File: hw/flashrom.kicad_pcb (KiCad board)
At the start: 2 copper layers, 22.9 x 52.1 mm, 12 parts, among them J1 Conn_01x03_Male, J3 Conn_01x03_Male, U1 Kickstart_Socket_A4000, U2 29F800

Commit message: convert project to kicad 7 format
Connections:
- net /~CE renamed /~{CE}
- net /~OE renamed /~{OE}
- net /~RESET renamed /~{RESET}
- net /~WE renamed /~{WE}
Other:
- net class Default removed
- board text added: "~{BUSY }WE ~{RESET}"
- board text removed: "~BUSY ~WE ~RESET"

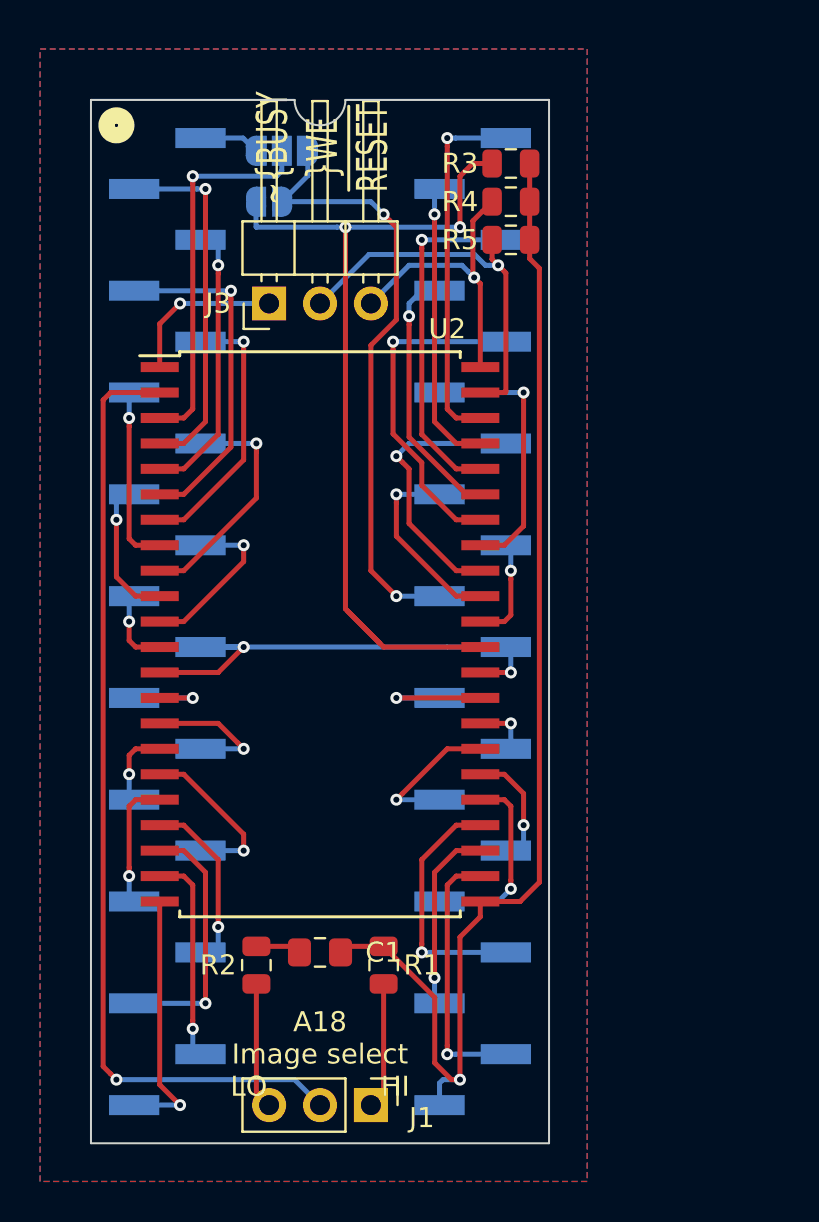
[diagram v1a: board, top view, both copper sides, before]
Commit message: switch flash to tsop, add tvs, and route pcb
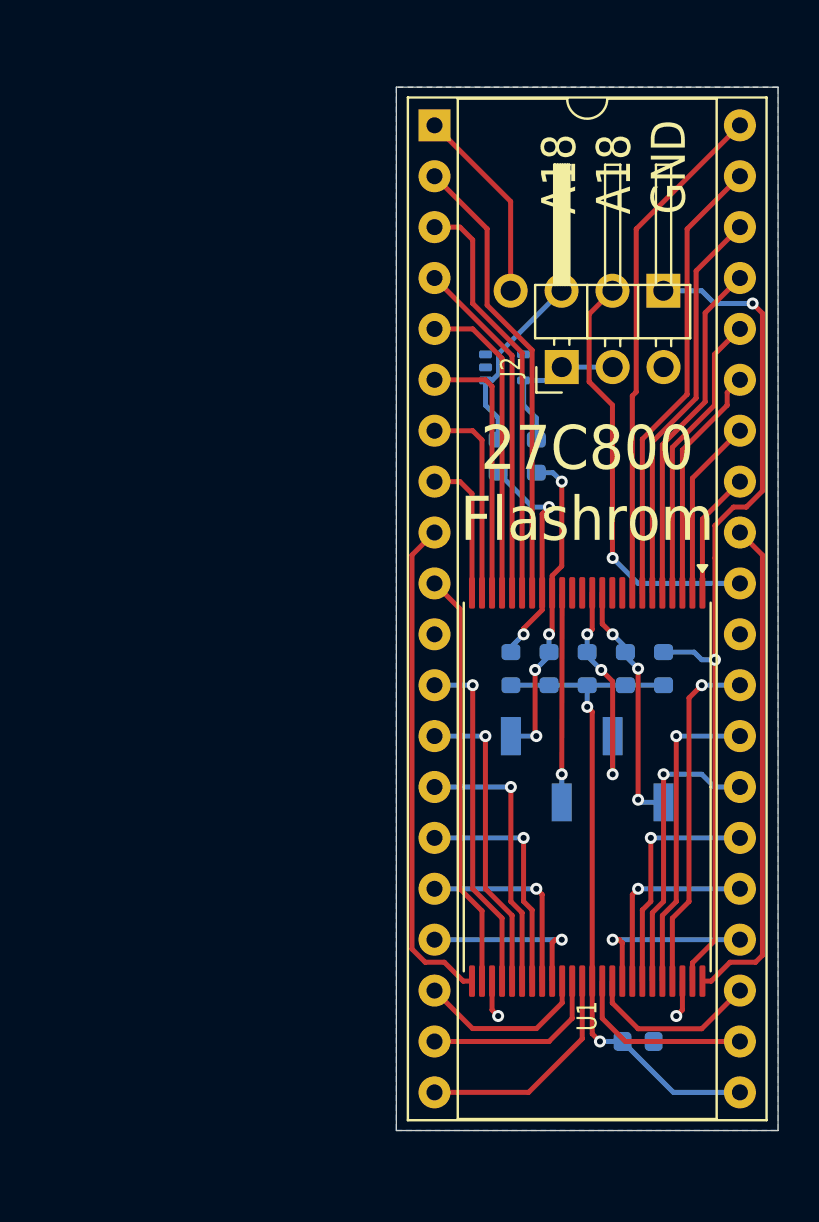
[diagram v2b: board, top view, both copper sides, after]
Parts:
- removed JP1: SolderJumper_3_Bridged12, Jumper:SolderJumper-3_P1.3mm_Open_RoundedPad1.0x1.5mm
- removed JP2: SolderJumper_2_Bridged, Jumper:SolderJumper-2_P1.3mm_Open_RoundedPad1.0x1.5mm
- added D1: NSQA6V8AW5T2G, Package_TO_SOT_SMD:SOT-353_SC-70-5, B.Cu at (54.3, 62.9)
- added J2: Conn_01x03_Pin, Connector_PinHeader_2.54mm:PinHeader_1x03_P2.54mm_Horizontal, F.Cu at (57.1, 62.9)
- added R6: 15k, Resistor_SMD:R_0603_1608Metric, B.Cu at (56.5, 77.9)
- added R7: 15k, Resistor_SMD:R_0603_1608Metric, B.Cu at (54.6, 77.9)
- C1: footprint Capacitor_SMD:C_0805_2012Metric_Pad1.15x1.40mm_HandSolder -> Capacitor_SMD:C_0603_1608Metric; moved to B.Cu
- J1: value Conn_01x03_Male -> Conn_01x04_Pin; footprint Connector_PinHeader_2.54mm:PinHeader_1x03_P2.54mm_Vertical -> Connector_PinHeader_2.54mm:PinHeader_1x04_P2.54mm_Horizontal; moved to B.Cu
- J3: value Conn_01x03_Male -> BG306-04-A-1-0400-L; footprint Connector_PinHeader_2.54mm:PinHeader_1x03_P2.54mm_Horizontal -> Connector_PinSocket_2.54mm:PinSocket_1x04_P2.54mm_Vertical_SMD_Pin1Left; moved to B.Cu
- R1, R2: value 10k -> 100; footprint Resistor_SMD:R_0805_2012Metric -> Resistor_SMD:R_0603_1608Metric; moved to B.Cu
- R3, R4, R5: value 10k -> 15k; footprint Resistor_SMD:R_0805_2012Metric -> Resistor_SMD:R_0603_1608Metric; moved to B.Cu
- U1: value Kickstart_Socket_A4000 -> 29F800-TSOP; footprint flashkick:DIP-40_W15.24mm_SMDHeader -> Package_SO:TSOP-I-48_18.4x12mm_P0.5mm; moved to F.Cu
- U2: value 29F800 -> Kickstart_Socket_A4000; footprint Package_SO:PSOP-44_16.9x27.17mm_P1.27mm -> Package_DIP:DIP-40_W15.24mm_Socket
- moved J1 43.2 mm to (62.2, 59.1), turned to 90 degrees
- moved R2 29.0 mm to (55.9, 67.3), turned to -90 degrees
- moved J3 28.1 mm to (58.4, 82.9)
- moved R3 26.3 mm to (62.2, 77.9), turned to -90 degrees
- moved U2 26.0 mm to (50.8, 50.8)
- moved R1 26.0 mm to (54.0, 67.3), turned to 90 degrees
- moved R4 24.0 mm to (60.3, 77.9), turned to -90 degrees
- moved R5 21.7 mm to (58.4, 77.9), turned to -90 degrees
- moved C1 16.5 mm to (61.0, 96.5), turned to 0 degrees
- moved U1 10.0 mm to (58.4, 83.8), turned to -90 degrees
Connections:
- J1 pad 1: Net-(J1-Pad1) -> /~{BYTE}
- J1 pad 2: /A18 -> /OA17
- J1 pad 3: Net-(J1-Pad3) -> /TVS1
- J3 pad 1: Net-(J3-Pad1) -> /~{WE}
- J3 pad 2: /~{WE} -> /~{RESET}
- J3 pad 3: /~{RESET} -> /RY/~{BY}
- R1 pad 1: +5V -> /A17
- R1 pad 2: Net-(J1-Pad1) -> /TVS1
- R2 pad 1: Net-(J1-Pad3) -> /TVS3
- R2 pad 2: GND -> /A18
- R3 pad 1: +5V -> /~{BYTE}
- R3 pad 2: Net-(JP2-Pad1) -> +5V
- R4 pad 1: +5V -> /~{WE}
- R4 pad 2: /~{RESET} -> +5V
- R5 pad 1: +5V -> /~{RESET}
- R5 pad 2: /~{WE} -> +5V
- U1 pad 1: /NA17 -> /A15
- U1 pad 10: /~{CE} -> unconnected-(U1-NC-Pad10)
- U1 pad 11: GND -> /~{WE}
- U1 pad 12: /~{OE} -> /~{RESET}
- U1 pad 13: /D0 -> unconnected-(U1-NC-Pad13)
- U1 pad 14: /D8 -> unconnected-(U1-NC-Pad14)
- U1 pad 15: /D1 -> /RY/~{BY}
- U1 pad 16: /D9 -> /A18
- U1 pad 17: /D2 -> /A17
- U1 pad 18: /D10 -> /A7
- U1 pad 19: /D3 -> /A6
- U1 pad 2: /A7 -> /A14
- U1 pad 20: /D11 -> /A5
- U1 pad 21: +5V -> /A4
- U1 pad 22: /D4 -> /A3
- U1 pad 23: /D12 -> /A2
- U1 pad 24: /D5 -> /A1
- U1 pad 25: /D13 -> /A0
- U1 pad 26: /D6 -> /~{CE}
- U1 pad 27: /D14 -> GND
- U1 pad 28: /D7 -> /~{OE}
- U1 pad 29: /D15 -> /D0
- U1 pad 3: /A6 -> /A13
- U1 pad 30: GND -> /D8
- U1 pad 31: /OA17 -> /D1
- U1 pad 32: /A16 -> /D9
- U1 pad 33: /A15 -> /D2
- U1 pad 34: /A14 -> /D10
- U1 pad 35: /A13 -> /D3
- U1 pad 36: /A12 -> /D11
- U1 pad 37: /A11 -> +5V
- U1 pad 38: /A10 -> /D4
- U1 pad 39: /A9 -> /D12
- U1 pad 4: /A5 -> /A12
- U1 pad 40: /A8 -> /D5
- U1 pad 5: /A4 -> /A11
- U1 pad 6: /A3 -> /A10
- U1 pad 7: /A2 -> /A9
- U1 pad 8: /A1 -> /A8
- U1 pad 9: /A0 -> unconnected-(U1-NC-Pad9)
- U2 pad 1: Net-(J3-Pad1) -> /NA17
- U2 pad 10: /A1 -> /~{CE}
- U2 pad 11: /A0 -> GND
- U2 pad 12: /~{CE} -> /~{OE}
- U2 pad 13: GND -> /D0
- U2 pad 14: /~{OE} -> /D8
- U2 pad 15: /D0 -> /D1
- U2 pad 16: /D8 -> /D9
- U2 pad 17: /D1 -> /D2
- U2 pad 18: /D9 -> /D10
- U2 pad 19: /D2 -> /D3
- U2 pad 2: /A18 -> /A7
- U2 pad 20: /D10 -> /D11
- U2 pad 21: /D3 -> +5V
- U2 pad 22: /D11 -> /D4
- U2 pad 23: +5V -> /D12
- U2 pad 24: /D4 -> /D5
- U2 pad 25: /D12 -> /D13
- U2 pad 26: /D5 -> /D6
- U2 pad 27: /D13 -> /D14
- U2 pad 28: /D6 -> /D7
- U2 pad 29: /D14 -> /D15
- U2 pad 3: /A17 -> /A6
- U2 pad 30: /D7 -> GND
- U2 pad 31: /D15 -> /OA17
- U2 pad 32: GND -> /A16
- U2 pad 33: Net-(JP2-Pad1) -> /A15
- U2 pad 34: /A16 -> /A14
- U2 pad 35: /A15 -> /A13
- U2 pad 36: /A14 -> /A12
- U2 pad 37: /A13 -> /A11
- U2 pad 38: /A12 -> /A10
- U2 pad 39: /A11 -> /A9
- U2 pad 4: /A7 -> /A5
- U2 pad 40: /A10 -> /A8
- U2 pad 5: /A6 -> /A4
- U2 pad 6: /A5 -> /A3
- U2 pad 7: /A4 -> /A2
- U2 pad 8: /A3 -> /A1
- U2 pad 9: /A2 -> /A0
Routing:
- net Net-(JP2-Pad1): track 44.7 -> 0.00 mm, vias 2 -> 0
- net /~{BYTE}: track 0.00 -> 43.3 mm, vias 0 -> 2
- net /A18: track 47.9 -> 16.0 mm, vias 1 -> 4
- net +5V: track 60.8 -> 33.7 mm, vias 1 -> 2
- net GND: track 27.3 -> 3.74 mm
- net /A16: track 5.25 -> 25.1 mm, vias 1 -> 0
- net /~{CE}: track 3.98 -> 20.8 mm, vias 1 -> 0
- net /A0: track 8.40 -> 24.9 mm, vias 1 -> 0
- net /D7: track 2.90 -> 15.7 mm
- net /~{OE}: track 5.36 -> 17.3 mm
- net /D15: track 6.34 -> 17.3 mm
- net /RY/~{BY}: track 0.00 -> 10.5 mm, vias 0 -> 1
- net /OA17: track 30.9 -> 21.2 mm, vias 2 -> 1
- net /TVS1: track 0.00 -> 9.46 mm
- net /D8: track 4.76 -> 13.7 mm
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- removed copper zone on F.Cu, net GND
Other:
- board size 22.9 x 52.1 mm -> 19 x 52.1 mm
- rule pad_to_mask_clearance: 0.051 -> 0.05
- rule solder_mask_min_width: 0.25 -> 0.15
- board text added: "27C800 Flashrom"
- board text added: "A18 A18 GND"
- board text added: "A18 RY/~{BY} ~{RESET} ~{WE}"
- board text added: "NA17 A17 OA17 ~{BYTE}"
- board text removed: "A18 Image select LO HI"
- board text removed: "Connect JP1/JP2 1-2 for programming/newer Amigas, JP1 2-3 for A500 rev 5/A2000 rev 4."
- board text removed: "~{BUSY }WE ~{RESET}"

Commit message: change pin 1 of j2 to /WE to support a wire for in-system programming
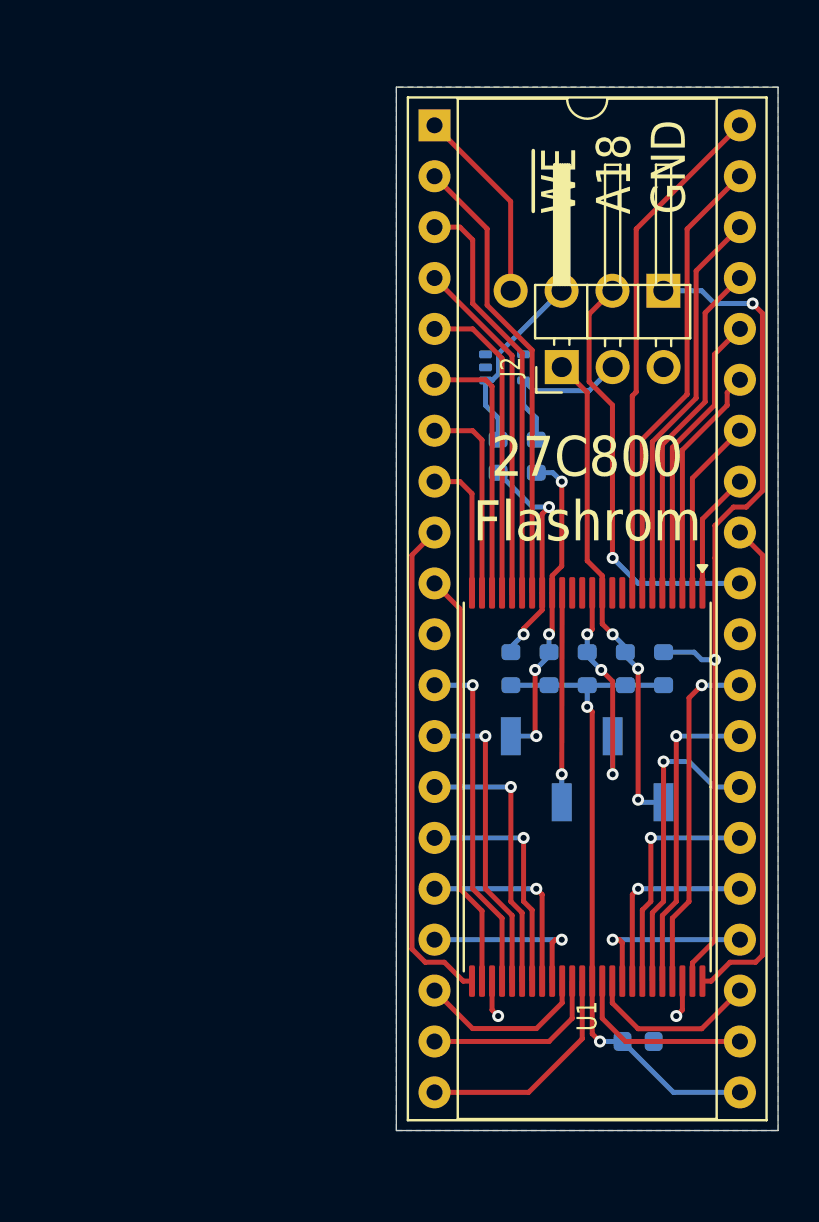
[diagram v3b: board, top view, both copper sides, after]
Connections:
- J2 pad 1: /TVS3 -> /~{WE}
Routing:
- net /~{WE}: track 12.4 -> 24.5 mm
- net /D14: track 14.6 -> 15.5 mm
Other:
- board text added: "~{WE} A18 GND"
- board text removed: "A18 A18 GND"

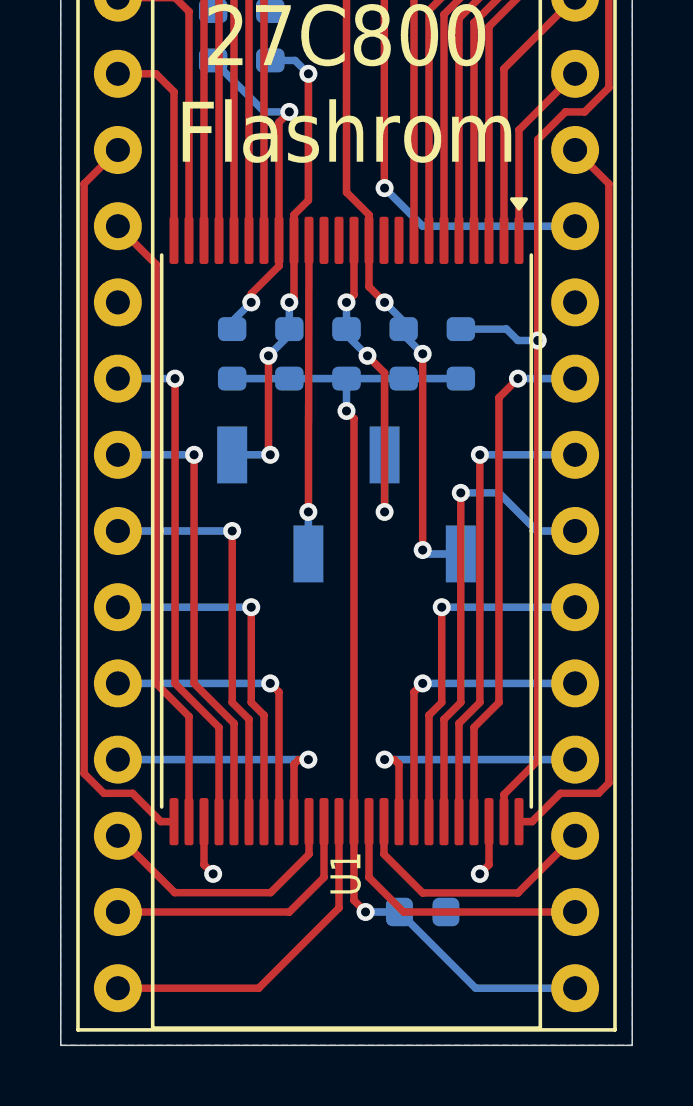
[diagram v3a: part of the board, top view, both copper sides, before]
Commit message: move c1 to f.cu for lesser inductance
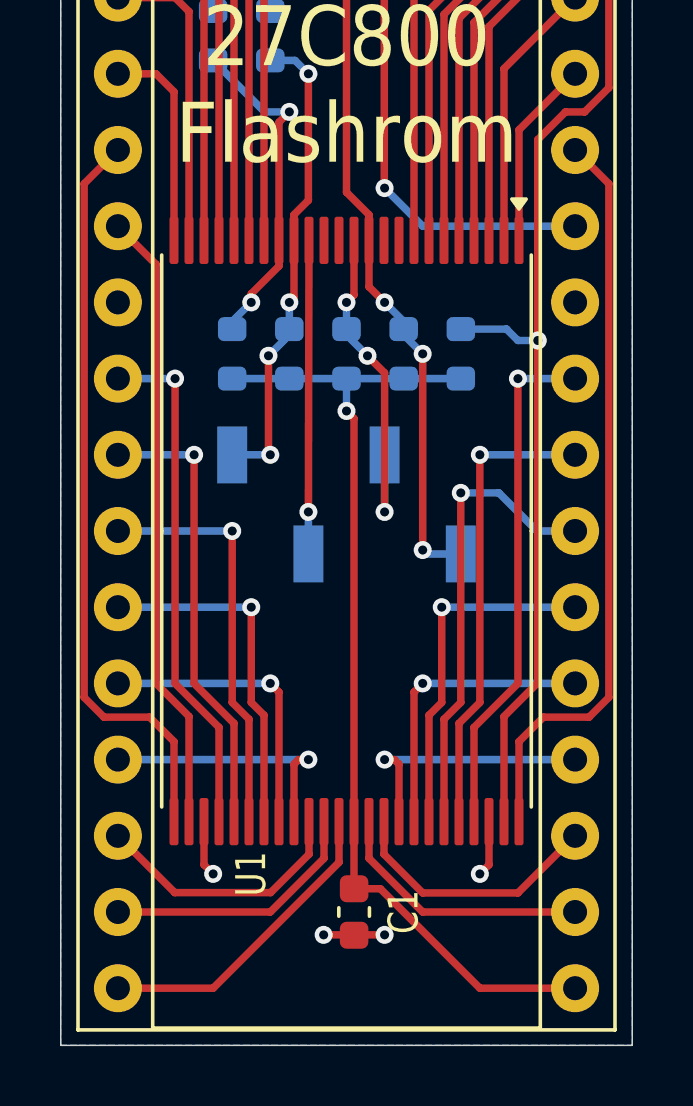
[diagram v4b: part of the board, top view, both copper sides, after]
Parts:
- C1: moved to F.Cu
- moved C1 2.29 mm to (58.7, 96.5), turned to -90 degrees
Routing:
- net GND: track 3.74 -> 5.78 mm, vias 2 -> 4
- net /D11: track 11.4 -> 10.5 mm
- net +5V: track 33.7 -> 33.5 mm, vias 2 -> 1
